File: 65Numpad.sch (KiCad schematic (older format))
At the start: 41 parts

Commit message: Matrix setup
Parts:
- added ALT, APOS, B, BKSLASH, BKSPC, COMMA, DEL, DOWN, EIGHT, ENTER, EQUALS, F, FIVE, FN, FOUR, G, H, HOME, I, J, K, L, LBRACE, LEFT, M, MINUS, N, NINE, O, P, PERIOD, PGDN, PGUP, R, RBRACE, RIGHT, SEMICOLON, SEVEN, SHIFT, SIX, SLASH, T, U, UP, V, Y, ZERO: MX-NoLED, symbol MX_Alps_Hybrid:MX-NoLED
- added D? (x47): 1N4148, Diode_THT:D_DO-35_SOD27_P7.62mm_Horizontal, symbol Diode:1N4148
- added POGO: Conn_01x04, symbol Connector_Generic:Conn_01x04
- gave numbers to parts that had none: 20
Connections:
- net COL0: now reaches ESC.1 (COL)
- net COL0: now also CAPS.1 (COL), CTRL.1 (COL), SHIFT.1 (COL), TAB.1 (COL)
- net ROW0: now reaches D?.1 (K)
- net ROW0: now also D?.1 (K), D?.1 (K), D?.1 (K), D?.1 (K), D?.1 (K), D?.1 (K), D?.1 (K), D?.1 (K), D?.1 (K), D?.1 (K), D?.1 (K), D?.1 (K), D?.1 (K)
- net COL1: now reaches ONE.1 (COL)
- net COL1: now also A.1 (COL), Q.1 (COL), WIN.1 (COL), Z.1 (COL)
- net COL2: now reaches TWO.1 (COL)
- net COL2: now also ALT.1 (COL), S.1 (COL), W.1 (COL), X.1 (COL)
- net COL3: now reaches THREE.1 (COL)
- net COL3: now also C.1 (COL), D.1 (COL), E.1 (COL), SPACE.1 (COL)
- net ROW1: now reaches D?.1 (K)
- net ROW1: now also D?.1 (K), D?.1 (K), D?.1 (K), D?.1 (K), D?.1 (K), D?.1 (K), D?.1 (K), D?.1 (K), D?.1 (K), D?.1 (K), D?.1 (K), D?.1 (K), D?.1 (K)
- net ROW2: now reaches D?.1 (K)
- net ROW2: now also D?.1 (K), D?.1 (K), D?.1 (K), D?.1 (K), D?.1 (K), D?.1 (K), D?.1 (K), D?.1 (K), D?.1 (K), D?.1 (K), D?.1 (K), D?.1 (K), D?.1 (K)
- net ROW3: now reaches D?.1 (K)
- net ROW3: now also D?.1 (K), D?.1 (K), D?.1 (K), D?.1 (K), D?.1 (K), D?.1 (K), D?.1 (K), D?.1 (K), D?.1 (K), D?.1 (K), D?.1 (K), D?.1 (K), D?.1 (K)
- net ROW4: now reaches D?.1 (K)
- net ROW4: now also D?.1 (K), D?.1 (K), D?.1 (K), D?.1 (K), D?.1 (K), D?.1 (K), D?.1 (K), D?.1 (K), D?.1 (K), D?.1 (K)
- new net: D?.2 (A), FOUR.2 (ROW)
- new net: D?.2 (A), FIVE.2 (ROW)
- new net: D?.2 (A), SIX.2 (ROW)
- new net: D?.2 (A), SEVEN.2 (ROW)
- new net: D?.2 (A), R.2 (ROW)
- new net: D?.2 (A), T.2 (ROW)
- new net: D?.2 (A), Y.2 (ROW)
- new net: D?.2 (A), U.2 (ROW)
- new net: D?.2 (A), F.2 (ROW)
- new net: D?.2 (A), G.2 (ROW)
- new net: D?.2 (A), H.2 (ROW)
- new net: D?.2 (A), J.2 (ROW)
- new net: D?.2 (A), V.2 (ROW)
- new net: B.2 (ROW), D?.2 (A)
- new net: D?.2 (A), N.2 (ROW)
- new net: D?.2 (A), M.2 (ROW)
- new net: ALT.2 (ROW), D?.2 (A)
- new net: D?.2 (A), FN.2 (ROW)
- new net: D?.2 (A), LEFT.2 (ROW)
- new net: D?.2 (A), DOWN.2 (ROW)
- new net: D?.2 (A), EIGHT.2 (ROW)
- new net: D?.2 (A), NINE.2 (ROW)
- new net: D?.2 (A), ZERO.2 (ROW)
- new net: D?.2 (A), MINUS.2 (ROW)
- new net: D?.2 (A), I.2 (ROW)
- new net: D?.2 (A), O.2 (ROW)
- new net: D?.2 (A), P.2 (ROW)
- new net: D?.2 (A), LBRACE.2 (ROW)
- new net: D?.2 (A), K.2 (ROW)
- new net: D?.2 (A), L.2 (ROW)
- new net: D?.2 (A), SEMICOLON.2 (ROW)
- new net: APOS.2 (ROW), D?.2 (A)
- new net: COMMA.2 (ROW), D?.2 (A)
- new net: D?.2 (A), PERIOD.2 (ROW)
- new net: D?.2 (A), SLASH.2 (ROW)
- new net: D?.2 (A), SHIFT.2 (ROW)
- new net: D?.2 (A), RIGHT.2 (ROW)
- new net: D?.2 (A), EQUALS.2 (ROW)
- new net: BKSPC.2 (ROW), D?.2 (A)
- new net: D?.2 (A), DEL.2 (ROW)
- new net: D?.2 (A), RBRACE.2 (ROW)
- new net: BKSLASH.2 (ROW), D?.2 (A)
- new net: D?.2 (A), HOME.2 (ROW)
- new net: D?.2 (A), ENTER.2 (ROW)
- new net: D?.2 (A), PGUP.2 (ROW)
- new net: D?.2 (A), UP.2 (ROW)
- new net: D?.2 (A), PGDN.2 (ROW)
- new net COL10: HOME.1 (COL), P.1 (COL), SEMICOLON.1 (COL), SLASH.1 (COL), ZERO.1 (COL)
- new net COL11: APOS.1 (COL), LBRACE.1 (COL), MINUS.1 (COL), SHIFT.1 (COL)
- new net COL12: ENTER.1 (COL), EQUALS.1 (COL), RBRACE.1 (COL), UP.1 (COL)
- new net COL13: BKSLASH.1 (COL), BKSPC.1 (COL), PGDN.1 (COL), PGUP.1 (COL)
- new net COL4: ALT.1 (COL), F.1 (COL), FOUR.1 (COL), R.1 (COL), V.1 (COL)
- new net COL5: B.1 (COL), FIVE.1 (COL), FN.1 (COL), G.1 (COL), T.1 (COL)
- new net COL6: H.1 (COL), LEFT.1 (COL), N.1 (COL), SIX.1 (COL), Y.1 (COL)
- new net COL7: DOWN.1 (COL), J.1 (COL), M.1 (COL), SEVEN.1 (COL), U.1 (COL)
- new net COL8: COMMA.1 (COL), EIGHT.1 (COL), I.1 (COL), K.1 (COL), RIGHT.1 (COL)
- new net COL9: DEL.1 (COL), L.1 (COL), NINE.1 (COL), O.1 (COL), PERIOD.1 (COL)
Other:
- moved on the sheet: A, ALT, C, CAPS, CTRL, D, D?, E, ESC, ONE, Q, S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

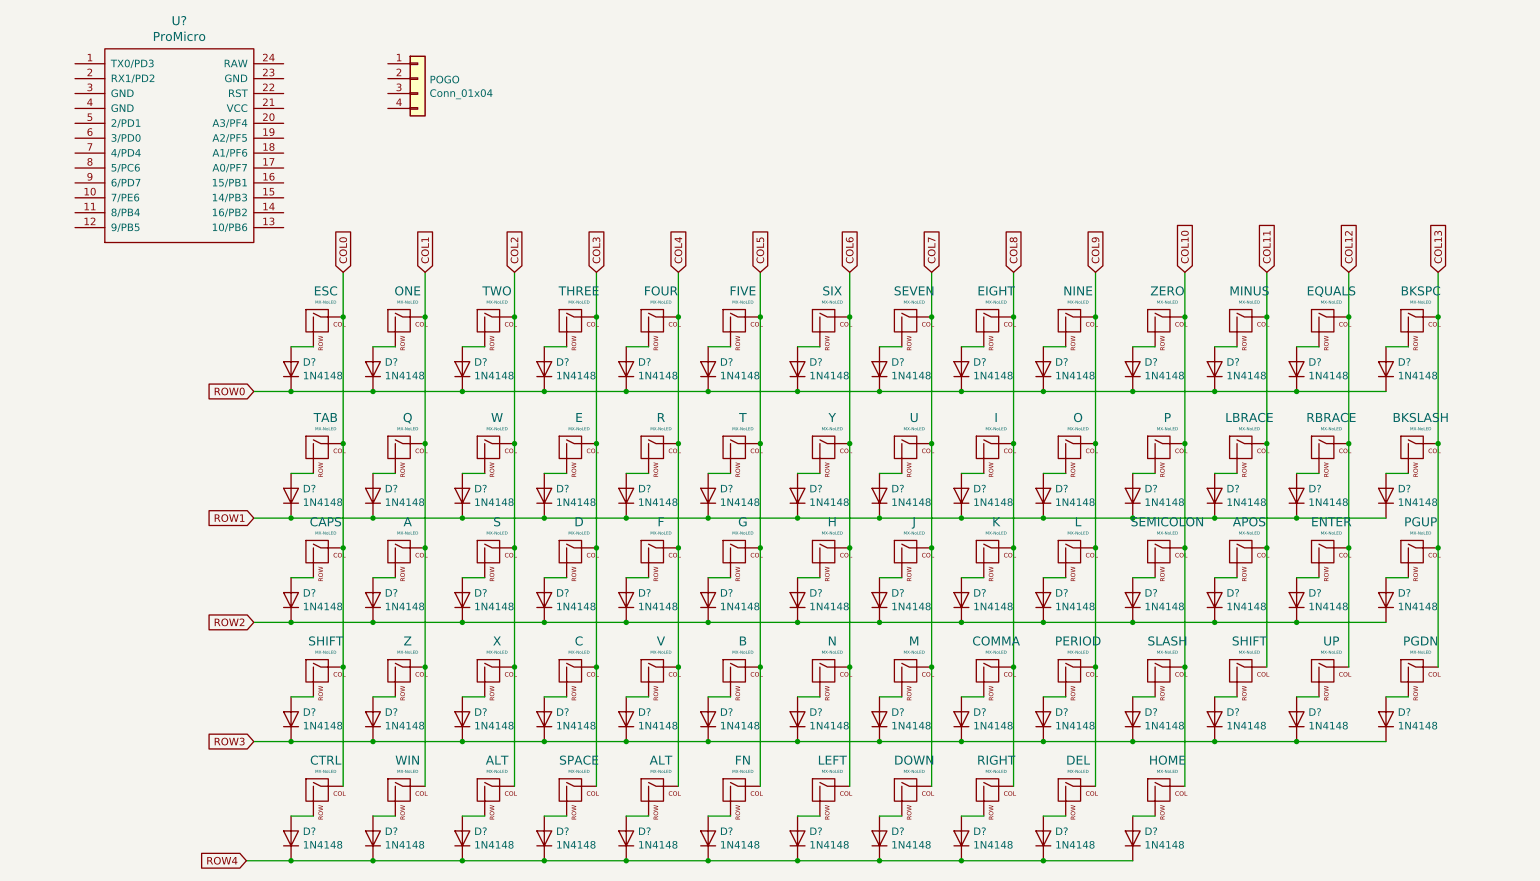
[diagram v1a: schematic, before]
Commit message: Duplex Matrix
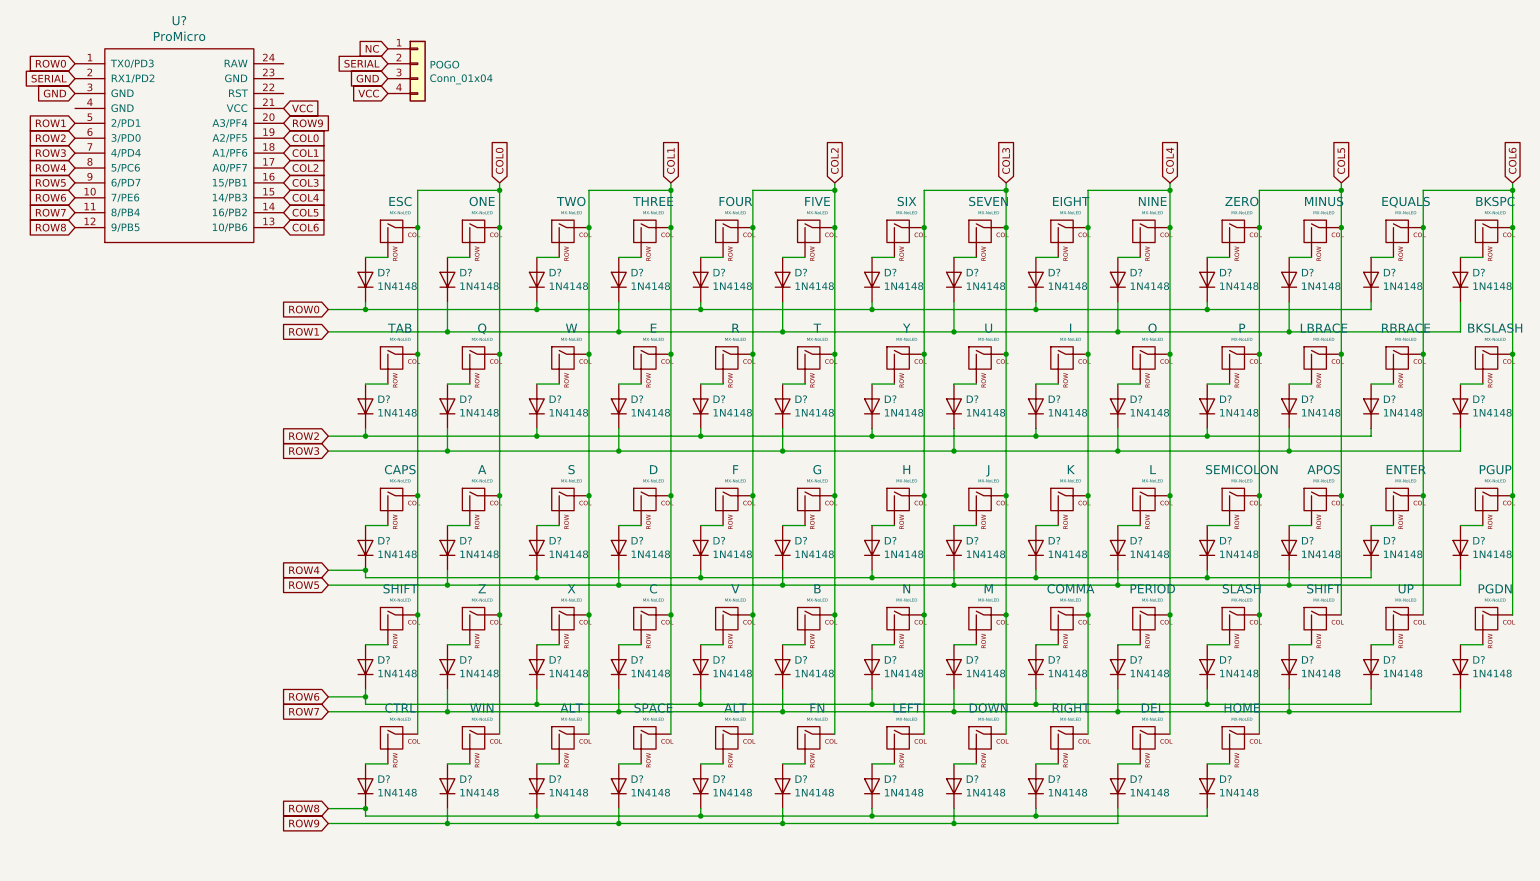
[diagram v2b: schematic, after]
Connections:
- net COL10 is gone; now on net COL5: HOME.1 (COL), P.1 (COL), SEMICOLON.1 (COL), SLASH.1 (COL), ZERO.1 (COL)
- net COL11 is gone; now on net COL5: APOS.1 (COL), LBRACE.1 (COL), MINUS.1 (COL), SHIFT.1 (COL)
- net COL12 is gone; now on net COL6: ENTER.1 (COL), EQUALS.1 (COL), RBRACE.1 (COL), UP.1 (COL)
- net COL13 is gone; now on net COL6: BKSLASH.1 (COL), BKSPC.1 (COL), PGDN.1 (COL), PGUP.1 (COL)
- net COL7 is gone; now on net COL3: DOWN.1 (COL), J.1 (COL), M.1 (COL), SEVEN.1 (COL), U.1 (COL)
- net COL8 is gone; now on net COL4: COMMA.1 (COL), EIGHT.1 (COL), I.1 (COL), K.1 (COL), RIGHT.1 (COL)
- net COL9 is gone; now on net COL4: DEL.1 (COL), L.1 (COL), NINE.1 (COL), O.1 (COL), PERIOD.1 (COL)
- net COL0: now also A.1 (COL), ONE.1 (COL), Q.1 (COL), U?.19 (A2/PF5), WIN.1 (COL), Z.1 (COL)
- net COL1: now also ALT.1 (COL), C.1 (COL), D.1 (COL), E.1 (COL), S.1 (COL), SPACE.1 (COL), THREE.1 (COL), TWO.1 (COL), U?.18 (A1/PF6), W.1 (COL), X.1 (COL); no longer A.1 (COL), ONE.1 (COL), Q.1 (COL), WIN.1 (COL), Z.1 (COL)
- net COL2: now also ALT.1 (COL), B.1 (COL), F.1 (COL), FIVE.1 (COL), FN.1 (COL), FOUR.1 (COL), G.1 (COL), R.1 (COL), T.1 (COL), U?.17 (A0/PF7), V.1 (COL); no longer ALT.1 (COL), S.1 (COL), TWO.1 (COL), W.1 (COL), X.1 (COL)
- net COL3: now also H.1 (COL), LEFT.1 (COL), N.1 (COL), SIX.1 (COL), U?.16 (15/PB1), Y.1 (COL); no longer C.1 (COL), D.1 (COL), E.1 (COL), SPACE.1 (COL), THREE.1 (COL)
- net COL4: now also U?.15 (14/PB3); no longer ALT.1 (COL), F.1 (COL), FOUR.1 (COL), R.1 (COL), V.1 (COL)
- net COL5: now also U?.14 (16/PB2); no longer B.1 (COL), FIVE.1 (COL), FN.1 (COL), G.1 (COL), T.1 (COL)
- net COL6: now also U?.13 (10/PB6); no longer H.1 (COL), LEFT.1 (COL), N.1 (COL), SIX.1 (COL), Y.1 (COL)
- net ROW0: now also U?.1 (TX0/PD3); no longer D?.1 (K), D?.1 (K), D?.1 (K), D?.1 (K), D?.1 (K), D?.1 (K), D?.1 (K)
- net ROW1: now also D?.1 (K), D?.1 (K), D?.1 (K), D?.1 (K), D?.1 (K), D?.1 (K), D?.1 (K), U?.5 (2/PD1); no longer D?.1 (K), D?.1 (K), D?.1 (K), D?.1 (K), D?.1 (K), D?.1 (K), D?.1 (K), D?.1 (K), D?.1 (K), D?.1 (K), D?.1 (K), D?.1 (K), D?.1 (K), D?.1 (K)
- net ROW2: now also D?.1 (K), D?.1 (K), D?.1 (K), D?.1 (K), D?.1 (K), D?.1 (K), D?.1 (K), U?.6 (3/PD0); no longer D?.1 (K), D?.1 (K), D?.1 (K), D?.1 (K), D?.1 (K), D?.1 (K), D?.1 (K), D?.1 (K), D?.1 (K), D?.1 (K), D?.1 (K), D?.1 (K), D?.1 (K), D?.1 (K)
- net ROW3: now also D?.1 (K), D?.1 (K), D?.1 (K), D?.1 (K), D?.1 (K), D?.1 (K), D?.1 (K), U?.7 (4/PD4); no longer D?.1 (K), D?.1 (K), D?.1 (K), D?.1 (K), D?.1 (K), D?.1 (K), D?.1 (K), D?.1 (K), D?.1 (K), D?.1 (K), D?.1 (K), D?.1 (K), D?.1 (K), D?.1 (K)
- net ROW4: now also D?.1 (K), D?.1 (K), D?.1 (K), D?.1 (K), D?.1 (K), D?.1 (K), D?.1 (K), U?.8 (5/PC6); no longer D?.1 (K), D?.1 (K), D?.1 (K), D?.1 (K), D?.1 (K), D?.1 (K), D?.1 (K), D?.1 (K), D?.1 (K), D?.1 (K), D?.1 (K)
- net ROW6: now reaches U?.10 (7/PE6)
- net ROW6: now also D?.1 (K), D?.1 (K), D?.1 (K), D?.1 (K), D?.1 (K), D?.1 (K), D?.1 (K)
- net ROW7: now reaches U?.11 (8/PB4)
- net ROW7: now also D?.1 (K), D?.1 (K), D?.1 (K), D?.1 (K), D?.1 (K), D?.1 (K), D?.1 (K)
- net ROW8: now reaches U?.12 (9/PB5)
- net ROW8: now also D?.1 (K), D?.1 (K), D?.1 (K), D?.1 (K), D?.1 (K), D?.1 (K)
- net SERIAL: now reaches U?.2 (RX1/PD2)
- net SERIAL: now also POGO.2 (Pin_2)
- net ROW9: now reaches U?.20 (A3/PF4)
- net ROW9: now also D?.1 (K), D?.1 (K), D?.1 (K), D?.1 (K), D?.1 (K)
- net VCC: now reaches U?.21 (VCC)
- net VCC: now also POGO.4 (Pin_4)
- net GND: now reaches U?.3 (GND)
- net GND: now also POGO.3 (Pin_3)
- net ROW5: now reaches U?.9 (6/PD7)
- net ROW5: now also D?.1 (K), D?.1 (K), D?.1 (K), D?.1 (K), D?.1 (K), D?.1 (K), D?.1 (K)
- net NC: now reaches POGO.1 (Pin_1)
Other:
- moved on the sheet: A, ALT, APOS, B, BKSLASH, BKSPC, C, CAPS, COMMA, CTRL, D, D?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

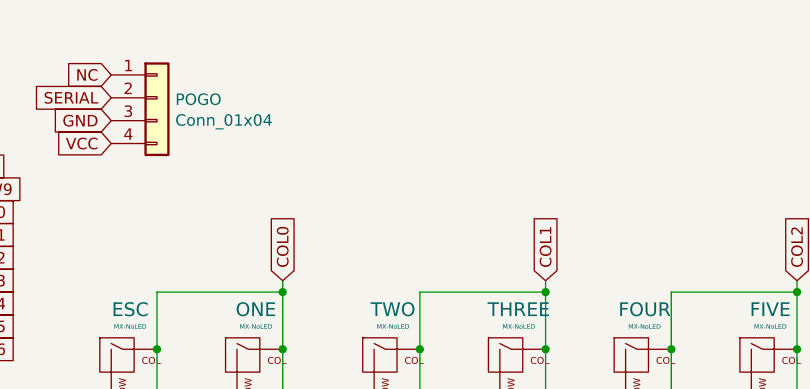
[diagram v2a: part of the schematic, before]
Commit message: Assign footprints
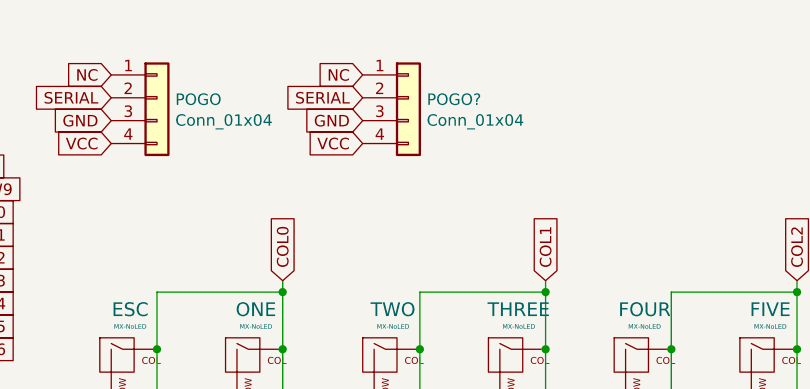
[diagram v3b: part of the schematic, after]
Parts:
- added POGO?: Conn_01x04, symbol Connector_Generic:Conn_01x04
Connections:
- net GND: now also POGO?.3 (Pin_3)
- net NC: now also POGO?.1 (Pin_1)
- net SERIAL: now also POGO?.2 (Pin_2)
- net VCC: now also POGO?.4 (Pin_4)
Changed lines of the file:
@@
 Wire Wire Line
 	2800 5250 2800 5200
+$Comp
+L Connector_Generic:Conn_01x04 POGO?
+U 1 1 5FEFD1CA
+P 4250 1000
+F 0 "POGO?" H 4330 992 50  0000 L CNN
+F 1 "Conn_01x04" H 4330 901 50  0000 L CNN
+F 2 "" H 4250 1000 50  0001 C CNN
+F 3 "~" H 4250 1000 50  0001 C CNN
+	1    4250 1000
+	1    0    0    -1
+$EndComp
+Text GLabel 4050 900  0    50   Input ~ 0
+NC
+Text GLabel 4050 1200 0    50   Input ~ 0
+VCC
+Text GLabel 4050 1000 0    50   Input ~ 0
+SERIAL
+Text GLabel 4050 1100 0    50   Input ~ 0
+GND
 $EndSCHEMATC
